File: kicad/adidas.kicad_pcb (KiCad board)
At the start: 2 copper layers, 152.7 x 107.2 mm, 4 parts

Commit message: add mpu6050 part (#4)
* add mpu6050 part

* add 6050 footprint
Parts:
- removed the G*** at (221.0, 91.4)
- added REF**: QFN50P400X400X95-24N, Library:QFN50P400X400X95-24N, B.Cu at (165.6, 99.6)
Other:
- board text added: "мне нравится двигать его двигать его"

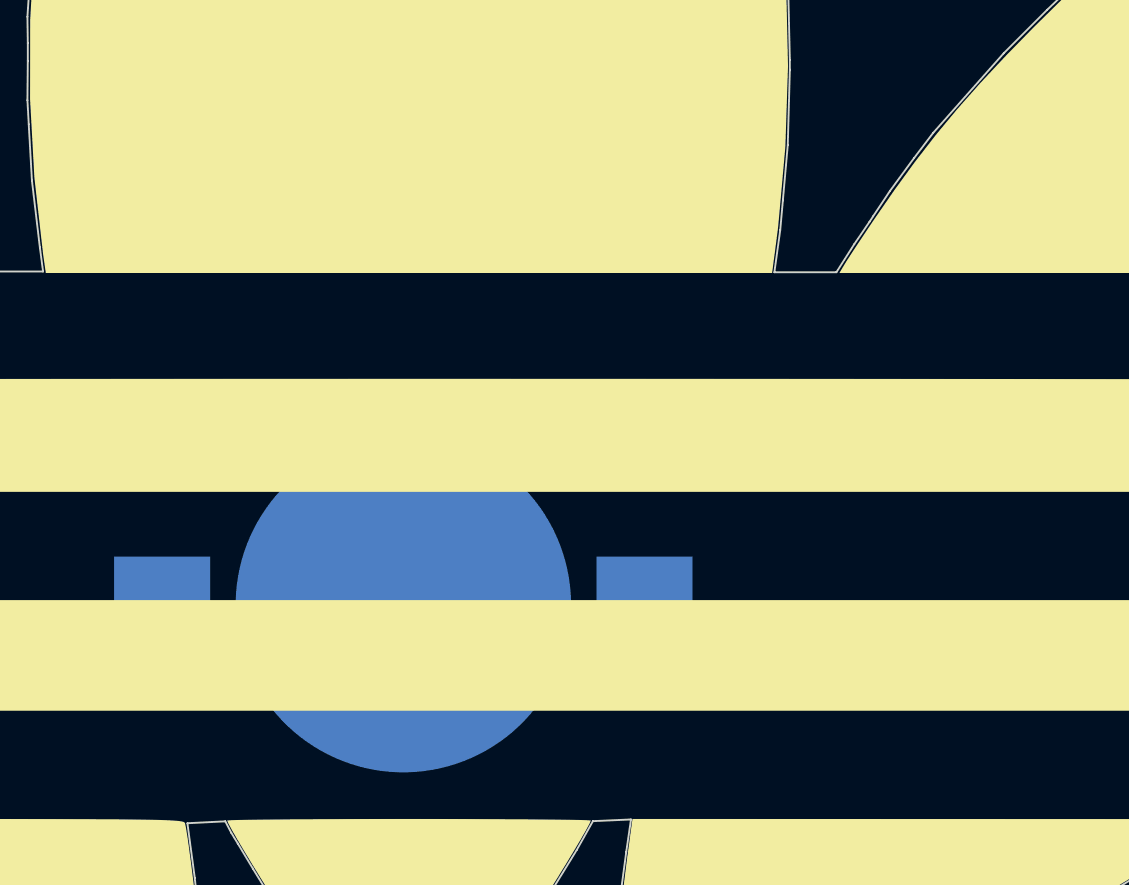
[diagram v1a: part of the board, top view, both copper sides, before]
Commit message: add a microcontroller
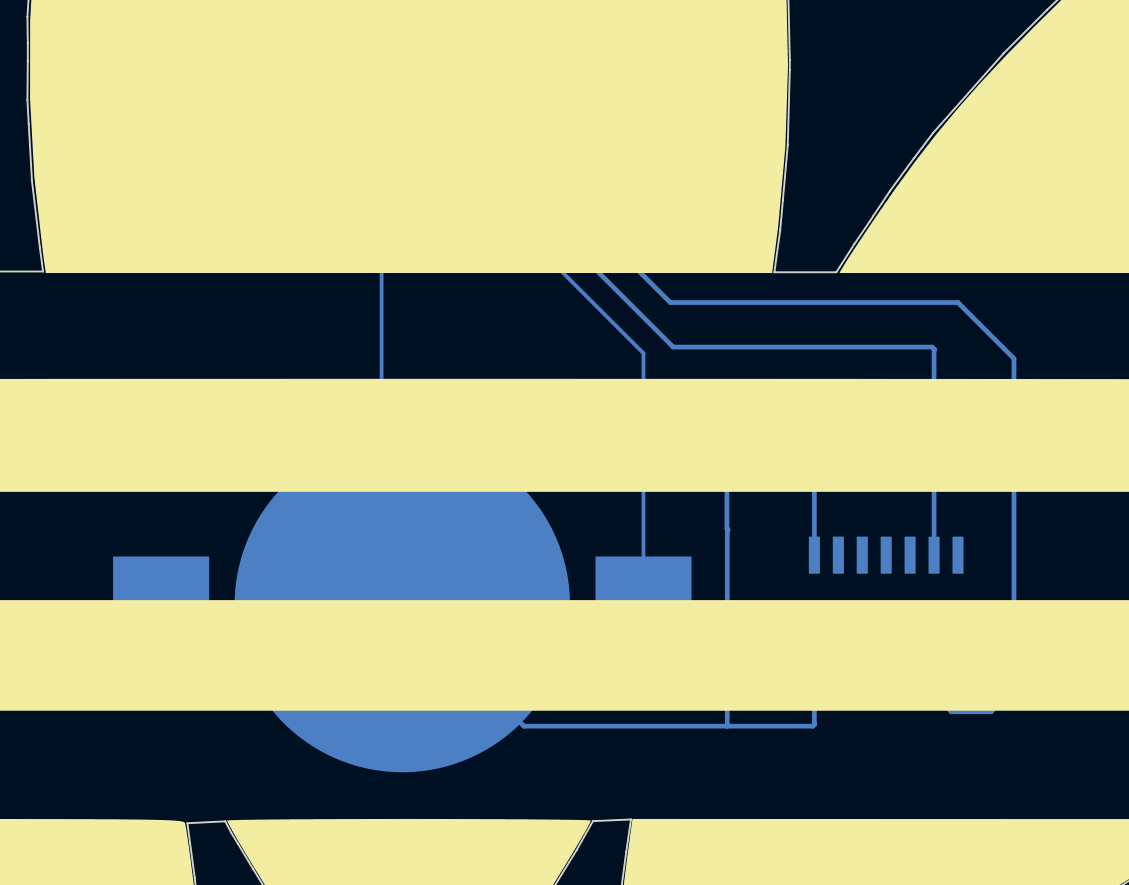
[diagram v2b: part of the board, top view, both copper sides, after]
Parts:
- added REF**: SOIC127P599X175-14N, at841:SOIC127P599X175-14N, B.Cu at (190.4, 120.2)
- added REF**: TestPoint_2Pads_Pitch2.54mm_Drill0.8mm, TestPoint:TestPoint_2Pads_Pitch2.54mm_Drill0.8mm, B.Cu at (182.0, 113.3)
- moved REF** 0.73 mm to (164.9, 99.4), turned to -90 degrees
- moved REF** 0.06 mm to (164.7, 120.4)
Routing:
- net (no net): track 0.00 -> 238.8 mm
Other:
- board text added: "+"
- board text added: "-"
- board text added: "Мощность"
- board text added: "приседать готов"
- board text removed: "мне нравится двигать его двигать его"

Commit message: test ISP header
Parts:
- added REF**: PinHeader_2x03_P2.54mm_Vertical, Connector_PinHeader_2.54mm:PinHeader_2x03_P2.54mm_Vertical, B.Cu at (187.1, 134.9)
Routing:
- net (no net): track 238.8 -> 340.2 mm, vias 0 -> 6
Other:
- board text added: "MISO"
- board text added: "MOSI"
- board text added: "SCK"
